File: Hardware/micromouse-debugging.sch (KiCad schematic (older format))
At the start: 1 part

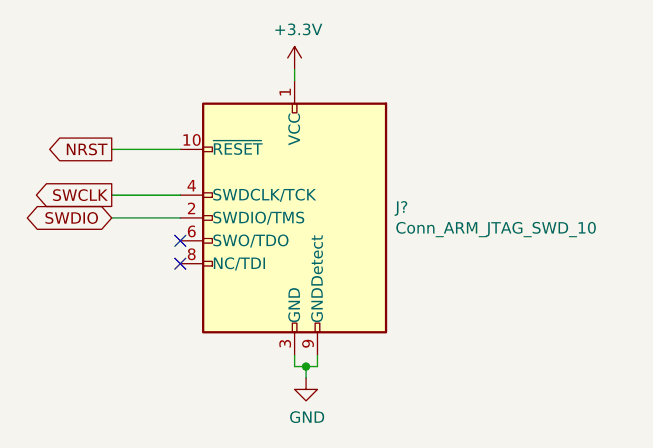
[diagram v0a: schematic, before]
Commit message: add power sub-schematic, fix some supply-connections, rearrange sub-schematics
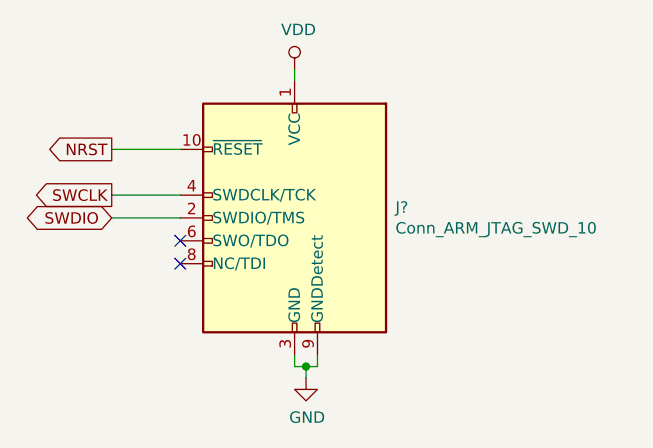
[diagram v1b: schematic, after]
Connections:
- net +3V3 renamed VDD
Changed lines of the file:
@@
 $Descr A4 11693 8268
 encoding utf-8
-Sheet 3 7
+Sheet 3 8
 Title ""
 Date ""
@@
 Wire Wire Line
 	5150 3650 4850 3650
+Wire Wire Line
+	5650 3300 5650 3350
+NoConn ~ 5150 4050
+NoConn ~ 5150 4150
 $Comp
-L power:+3.3V #PWR?
-U 1 1 5C9344F3
+L power:VDD #PWR?
+U 1 1 5C8C2900
 P 5650 3300
-AR Path="/5C9344F3" Ref="#PWR?"  Part="1"
-AR Path="/5C92AF24/5C9344F3" Ref="#PWR?"  Part="1"
 F 0 "#PWR?" H 5650 3150 50  0001 C CNN
-F 1 "+3.3V" H 5665 3473 50  0000 C CNN
+F 1 "VDD" H 5667 3473 50  0000 C CNN
 F 2 "" H 5650 3300 50  0001 C CNN
 F 3 "" H 5650 3300 50  0001 C CNN
@@
 	1    0    0    -1
 $EndComp
-Wire Wire Line
-	5650 3300 5650 3350
-NoConn ~ 5150 4050
-NoConn ~ 5150 4150
 $EndSCHEMATC

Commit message: [OLED]  - added kicad display lib for ssd1306 oled display footorint  - added ssd1306 schematic part  - added display plus signals into micromouse schematics
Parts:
- J?: symbol Connector:Conn_ARM_JTAG_SWD_10 -> micromouse-rescue:Conn_ARM_JTAG_SWD_10-Connector-micromouse-rescue
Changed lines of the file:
@@
 $Descr A4 11693 8268
 encoding utf-8
-Sheet 3 8
+Sheet 3 9
 Title ""
 Date ""
@@
 $EndDescr
 $Comp
-L Connector:Conn_ARM_JTAG_SWD_10 J?
+L micromouse-rescue:Conn_ARM_JTAG_SWD_10-Connector-micromouse-rescue J?
 U 1 1 5C9344DA
 P 5650 3950
